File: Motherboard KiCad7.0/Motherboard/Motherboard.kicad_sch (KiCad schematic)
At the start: 74 parts, among them J1 USB_B_Micro, J2 SWD_01x04_Pin, J3 2-1445057-2, J4 2-1445057-2, J5 2-1445057-2, J6 2-1445057-2, J7 2-1445057-2, Q1 AO3400A, Q2 AO3400A, Q3 AO3400A, Q4 AO3400A, Q5 AO3400A, Q6 AO3400A, SW1 SW_STM_RESET, SW2 SW_STM_BOOT_MODE, U1 STM32F103CBT6, U2 AMS1117-3.3, U3 LM66100DCKR, U4 LM66100DCKR, U5 LM66100DCKR, Y1 X322516MMB4SI

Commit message: Added screwswitch and subsheet
Added screwswitch symbol and created a subsheet to place the rest of the circuit components into
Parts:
- removed BZ1: PKM13EPYH4000, footprints:Buzzer_12.6x9.5RM5.0, symbol Device:Buzzer
- removed D1, D10, D2, D6, D7, D8, D9: 1N5819WS, Diode_SMD:D_SOD-323, symbol Diode:1N5819WS
- removed D5: WS2812B, LED_SMD:LED_WS2812B_PLCC4_5.0x5.0mm_P3.2mm, symbol LED:WS2812B
- removed J3, J4, J5, J6, J7: 2-1445057-2, CONN_2-1445057-2_TYCO, symbol CONN_2-1445057-2_TYCO:2-1445057-2
- removed Q1, Q2, Q3, Q4, Q5, Q6: AO3400A, Package_TO_SOT_SMD:SOT-23, symbol Transistor_FET:AO3400A
- removed R10, R12, R14, R16, R18, R4: 510R, Resistor_SMD:R_0603_1608Metric, symbol Device:R
- removed R11, R13, R15, R17, R5, R9: 10k, Resistor_SMD:R_0603_1608Metric, symbol Device:R
- removed R7: 1k, Resistor_SMD:R_0603_1608Metric, symbol Device:R
- added C17: 4.7uF, Capacitor_SMD:C_0805_2012Metric, symbol Device:C
- added C18, C19: 100nF, Capacitor_SMD:C_0603_1608Metric, symbol Device:C
- added C20, C21: 22uF, Capacitor_SMD:C_0805_2012Metric, symbol Device:C
- added C22: 100uF, Capacitor_SMD:CP_Elec_6.3x5.9, symbol Device:C_Polarized
- added D11: WS2812B, LED_SMD:LED_WS2812B_PLCC4_5.0x5.0mm_P3.2mm, symbol LED:WS2812B
- added L1: 5.6uH, Inductor_SMD:L_Bourns_SRN8040TA, symbol Device:L
- added R19: 100k, Resistor_SMD:R_0603_1608Metric, symbol Device:R
- added R20: 22k, Resistor_SMD:R_0603_1608Metric, symbol Device:R
- added TP8: TP_BATT1, TestPoint:TestPoint_Pad_2.0x2.0mm, symbol Connector:TestPoint
- added TP9: TP_3.3V_A, TestPoint:TestPoint_Pad_2.0x2.0mm, symbol Connector:TestPoint
- added U6: LMR51430XDDCR, Package_TO_SOT_SMD:SOT-23-6_Handsoldering, symbol QRET_Buck_PSU-symbols:LMR51430XDDCR
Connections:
- net +3.3V: no longer D3.1 (VDD)
- net +BATT: now also C17.1, C18.1, TP8.1, U6.3 (VIN), U6.5 (EN)
- net GND: now also C17.2, C18.2, C20.2, C21.2, C22.2, D11.3 (VSS), R20.2, U6.1 (GND)
- net at D3.2 (DOUT): now also D11.4 (DIN)
- new net: C19.1, L1.1, U6.2 (SW)
- new net: C19.2, U6.6 (CB)
- new net: R19.2, R20.1, U6.4 (FB)
- new net 3.3V_A: C20.1, C21.1, C22.1, D11.1 (VDD), D3.1 (VDD), L1.2, R19.1, TP9.1
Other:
- added sheet Motherboard P2 (Motherboard P2.kicad_sch)
- note added: "FOLLOW LAYOUT EXAMPLE (9.4.2) FROM DATASHEET LMR51430: PFM @ 500kHz (simpler routing & higher efficiency)"
- note added: "Max Output: 2.5A"
- note added: "Primary 3.3V Buck Regulator"
- note added: "Rfbt=100k, Rfbb=22k Vout = ((Rfbt*0.6)/Rfbb)+0.6 Vout = 3.327V"
- note removed: "Air Pump"
- note removed: "Buzzer"
- note removed: "Solenoid Valves"
- moved on the sheet: C1, J2, R2, SW1

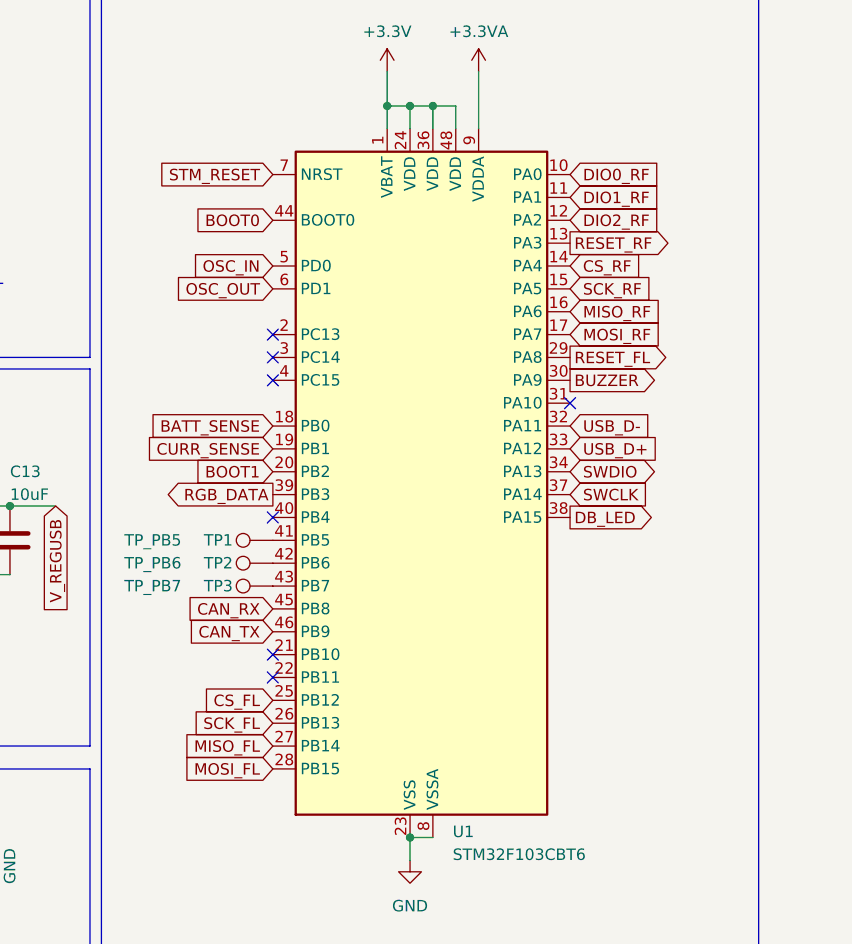
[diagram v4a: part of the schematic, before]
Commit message: Updated STM32 pinout
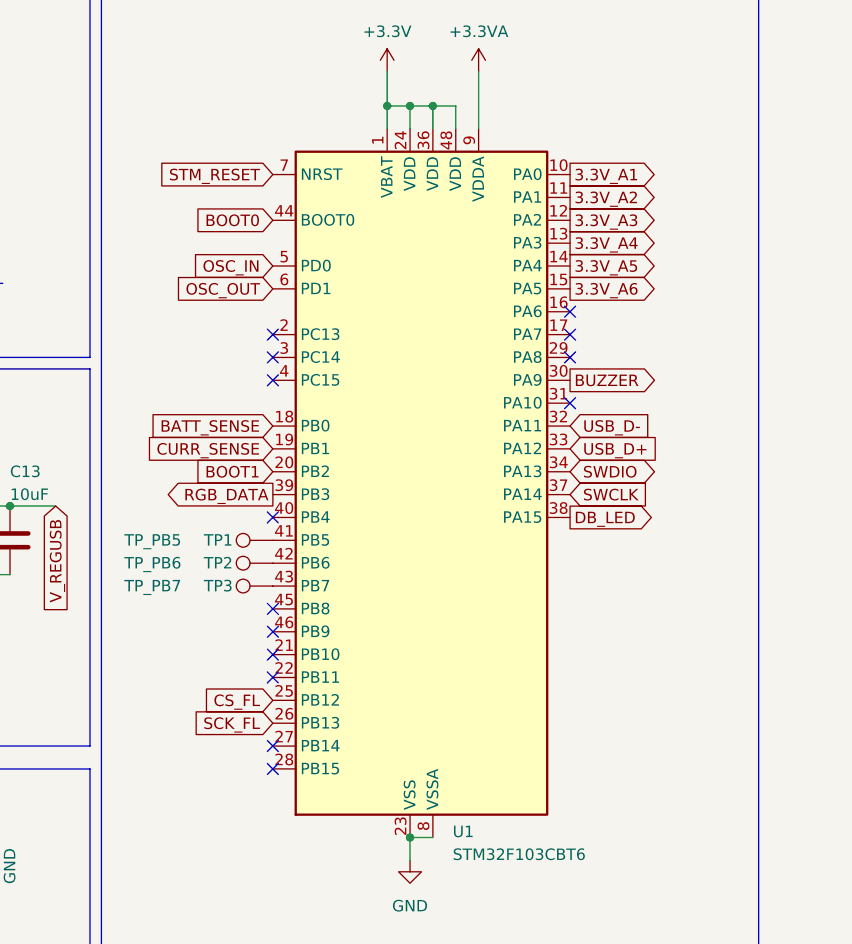
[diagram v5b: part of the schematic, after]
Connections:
- net CAN_RX: no longer names the net of U1.45 (PB8)
- net CAN_TX: no longer names the net of U1.46 (PB9)
- net CS_RF renamed 3.3V_A5
- net DIO0_RF renamed 3.3V_A1
- net DIO1_RF renamed 3.3V_A2
- net DIO2_RF renamed 3.3V_A3
- net MISO_FL: no longer names the net of U1.27 (PB14)
- net MISO_RF: no longer names the net of U1.16 (PA6)
- net MOSI_FL: no longer names the net of U1.28 (PB15)
- net MOSI_RF: no longer names the net of U1.17 (PA7)
- net RESET_FL: no longer names the net of U1.29 (PA8)
- net RESET_RF renamed 3.3V_A4
- net SCK_RF renamed 3.3V_A6
- no-connect marks 10 -> 17
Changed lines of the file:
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@@
   (junction (at 247.65 29.21) (diameter 0) (color 0 0 0 0)
   )
+  (no_connect (at 229.87 100.33))
   (no_connect (at 132.08 38.1))
+  (no_connect (at 229.87 87.63))
   (no_connect (at 229.87 59.69))
+  (no_connect (at 229.87 85.09))
   (no_connect (at 229.87 92.71))
   (no_connect (at 229.87 74.93))
+  (no_connect (at 229.87 102.87))
   (no_connect (at 162.56 83.82))
+  (no_connect (at 262.89 57.15))
+  (no_connect (at 262.89 52.07))
   (no_connect (at 262.89 62.23))
   (no_connect (at 229.87 54.61))
+  (no_connect (at 262.89 54.61))
   (no_connect (at 152.4 88.9))
   (no_connect (at 229.87 90.17))
@@
     )
   )
-  (global_label "RESET_RF" (shape output) (at 262.89 44.45 0) (fields_autoplaced)
-    (effects (font (size 1.27 1.27)) (justify left))
-    (property "Intersheetrefs" "${INTERSHEET_REFS}" (at 274.9465 44.45 0)
-      (effects (font (size 1.27 1.27)) (justify left) hide)
-    )
-  )
   (global_label "DB_LED" (shape input) (at 97.155 66.675 180) (fields_autoplaced)
     (effects (font (size 1.27 1.27)) (justify right))
@@
     )
   )
-  (global_label "CAN_RX" (shape input) (at 229.87 85.09 180) (fields_autoplaced)
-    (effects (font (size 1.27 1.27)) (justify right))
-    (property "Intersheetrefs" "${INTERSHEET_REFS}" (at 219.7486 85.09 0)
-      (effects (font (size 1.27 1.27)) (justify right) hide)
-    )
-  )
   (global_label "V_REGUSB" (shape input) (at 205.74 73.66 270) (fields_autoplaced)
     (effects (font (size 1.27 1.27)) (justify right))
@@
     )
   )
+  (global_label "3.3V_A1" (shape output) (at 262.89 36.83 0) (fields_autoplaced)
+    (effects (font (size 1.27 1.27)) (justify left))
+    (property "Intersheetrefs" "${INTERSHEET_REFS}" (at 273.2533 36.83 0)
+      (effects (font (size 1.27 1.27)) (justify left) hide)
+    )
+  )
   (global_label "OSC_OUT" (shape input) (at 229.87 49.53 180) (fields_autoplaced)
     (effects (font (size 1.27 1.27)) (justify right))
@@
     )
   )
-  (global_label "MISO_RF" (shape input) (at 262.89 52.07 0) (fields_autoplaced)
-    (effects (font (size 1.27 1.27)) (justify left))
-    (property "Intersheetrefs" "${INTERSHEET_REFS}" (at 273.7976 52.07 0)
-      (effects (font (size 1.27 1.27)) (justify left) hide)
-    )
-  )
-  (global_label "CAN_TX" (shape input) (at 229.87 87.63 180) (fields_autoplaced)
-    (effects (font (size 1.27 1.27)) (justify right))
-    (property "Intersheetrefs" "${INTERSHEET_REFS}" (at 220.051 87.63 0)
-      (effects (font (size 1.27 1.27)) (justify right) hide)
-    )
-  )
   (global_label "SCK_FL" (shape input) (at 229.87 97.79 180) (fields_autoplaced)
     (effects (font (size 1.27 1.27)) (justify right))
@@
     )
   )
-  (global_label "MOSI_RF" (shape input) (at 262.89 54.61 0) (fields_autoplaced)
-    (effects (font (size 1.27 1.27)) (justify left))
-    (property "Intersheetrefs" "${INTERSHEET_REFS}" (at 273.7976 54.61 0)
-      (effects (font (size 1.27 1.27)) (justify left) hide)
-    )
-  )
   (global_label "SWCLK" (shape input) (at 262.89 72.39 0) (fields_autoplaced)
     (effects (font (size 1.27 1.27)) (justify left))
@@
     )
   )
-  (global_label "RESET_FL" (shape output) (at 262.89 57.15 0) (fields_autoplaced)
-    (effects (font (size 1.27 1.27)) (justify left))
-    (property "Intersheetrefs" "${INTERSHEET_REFS}" (at 274.7046 57.15 0)
+  (global_label "3.3V_A3" (shape output) (at 262.89 41.91 0) (fields_autoplaced)
+    (effects (font (size 1.27 1.27)) (justify left))
+    (property "Intersheetrefs" "${INTERSHEET_REFS}" (at 273.2533 41.91 0)
       (effects (font (size 1.27 1.27)) (justify left) hide)
     )
@@
     )
   )
-  (global_label "DIO0_RF" (shape input) (at 262.89 36.83 0) (fields_autoplaced)
-    (effects (font (size 1.27 1.27)) (justify left))
-    (property "Intersheetrefs" "${INTERSHEET_REFS}" (at 273.6162 36.83 0)
+  (global_label "3.3V_A4" (shape output) (at 262.89 44.45 0) (fields_autoplaced)
+    (effects (font (size 1.27 1.27)) (justify left))
+    (property "Intersheetrefs" "${INTERSHEET_REFS}" (at 273.2533 44.45 0)
       (effects (font (size 1.27 1.27)) (justify left) hide)
     )
@@
     )
   )
-  (global_label "DIO1_RF" (shape input) (at 262.89 39.37 0) (fields_autoplaced)
-    (effects (font (size 1.27 1.27)) (justify left))
-    (property "Intersheetrefs" "${INTERSHEET_REFS}" (at 273.6162 39.37 0)
-      (effects (font (size 1.27 1.27)) (justify left) hide)
-    )
-  )
-  (global_label "DIO2_RF" (shape input) (at 262.89 41.91 0) (fields_autoplaced)
-    (effects (font (size 1.27 1.27)) (justify left))
-    (property "Intersheetrefs" "${INTERSHEET_REFS}" (at 273.6162 41.91 0)
-      (effects (font (size 1.27 1.27)) (justify left) hide)
-    )
-  )
   (global_label "STM_RESET" (shape output) (at 66.04 176.53 0) (fields_autoplaced)
     (effects (font (size 1.27 1.27)) (justify left))
@@
     )
   )
-  (global_label "CS_RF" (shape input) (at 262.89 46.99 0) (fields_autoplaced)
-    (effects (font (size 1.27 1.27)) (justify left))
-    (property "Intersheetrefs" "${INTERSHEET_REFS}" (at 271.6809 46.99 0)
+  (global_label "3.3V_A5" (shape output) (at 262.89 46.99 0) (fields_autoplaced)
+    (effects (font (size 1.27 1.27)) (justify left))
+    (property "Intersheetrefs" "${INTERSHEET_REFS}" (at 273.2533 46.99 0)
       (effects (font (size 1.27 1.27)) (justify left) hide)
     )
@@
     )
   )
-  (global_label "MOSI_FL" (shape input) (at 229.87 102.87 180) (fields_autoplaced)
-    (effects (font (size 1.27 1.27)) (justify right))
-    (property "Intersheetrefs" "${INTERSHEET_REFS}" (at 219.2043 102.87 0)
-      (effects (font (size 1.27 1.27)) (justify right) hide)
-    )
-  )
   (global_label "3.3V_A" (shape input) (at 101.6 30.48 180) (fields_autoplaced)
     (effects (font (size 1.27 1.27)) (justify right))
@@
     )
   )
-  (global_label "MISO_FL" (shape input) (at 229.87 100.33 180) (fields_autoplaced)
-    (effects (font (size 1.27 1.27)) (justify right))
-    (property "Intersheetrefs" "${INTERSHEET_REFS}" (at 219.2043 100.33 0)
-      (effects (font (size 1.27 1.27)) (justify right) hide)
-    )
-  )
   (global_label "BOOT0" (shape input) (at 229.87 41.91 180) (fields_autoplaced)
     (effects (font (size 1.27 1.27)) (justify right))
@@
     )
   )
+  (global_label "3.3V_A6" (shape output) (at 262.89 49.53 0) (fields_autoplaced)
+    (effects (font (size 1.27 1.27)) (justify left))
+    (property "Intersheetrefs" "${INTERSHEET_REFS}" (at 273.2533 49.53 0)
+      (effects (font (size 1.27 1.27)) (justify left) hide)
+    )
+  )
   (global_label "SWCLK" (shape input) (at 49.53 144.78 180) (fields_autoplaced)
     (effects (font (size 1.27 1.27)) (justify right))
@@
     )
   )
-  (global_label "SCK_RF" (shape input) (at 262.89 49.53 0) (fields_autoplaced)
-    (effects (font (size 1.27 1.27)) (justify left))
-    (property "Intersheetrefs" "${INTERSHEET_REFS}" (at 272.9509 49.53 0)
-      (effects (font (size 1.27 1.27)) (justify left) hide)
-    )
-  )
   (global_label "USB_D-" (shape input) (at 165.1 81.28 270) (fields_autoplaced)
     (effects (font (size 1.27 1.27)) (justify right))
@@
     )
   )
+  (global_label "3.3V_A2" (shape output) (at 262.89 39.37 0) (fields_autoplaced)
+    (effects (font (size 1.27 1.27)) (justify left))
+    (property "Intersheetrefs" "${INTERSHEET_REFS}" (at 273.2533 39.37 0)
+      (effects (font (size 1.27 1.27)) (justify left) hide)
+    )
+  )

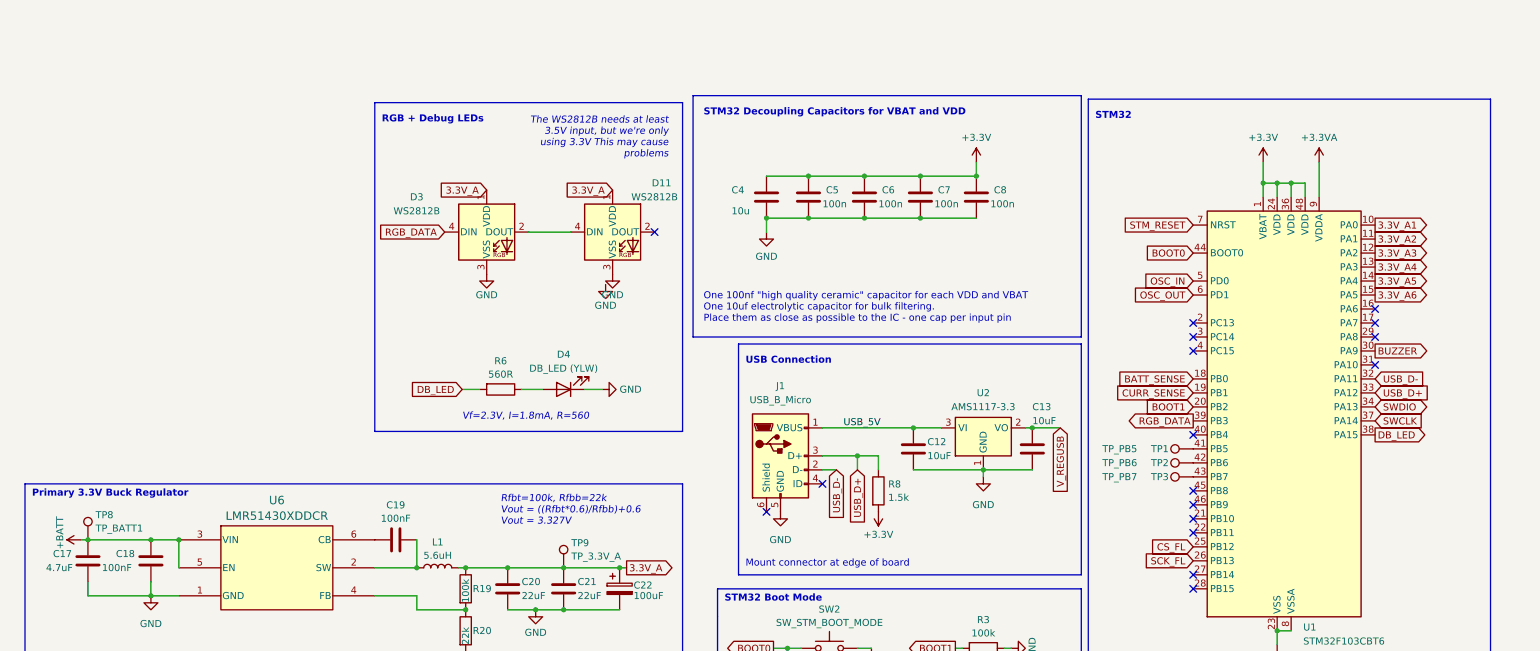
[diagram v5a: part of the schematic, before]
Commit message: Updated power connectors
Updated power connectors. Updated symbols and footprints for all components copied from avionics communications module.
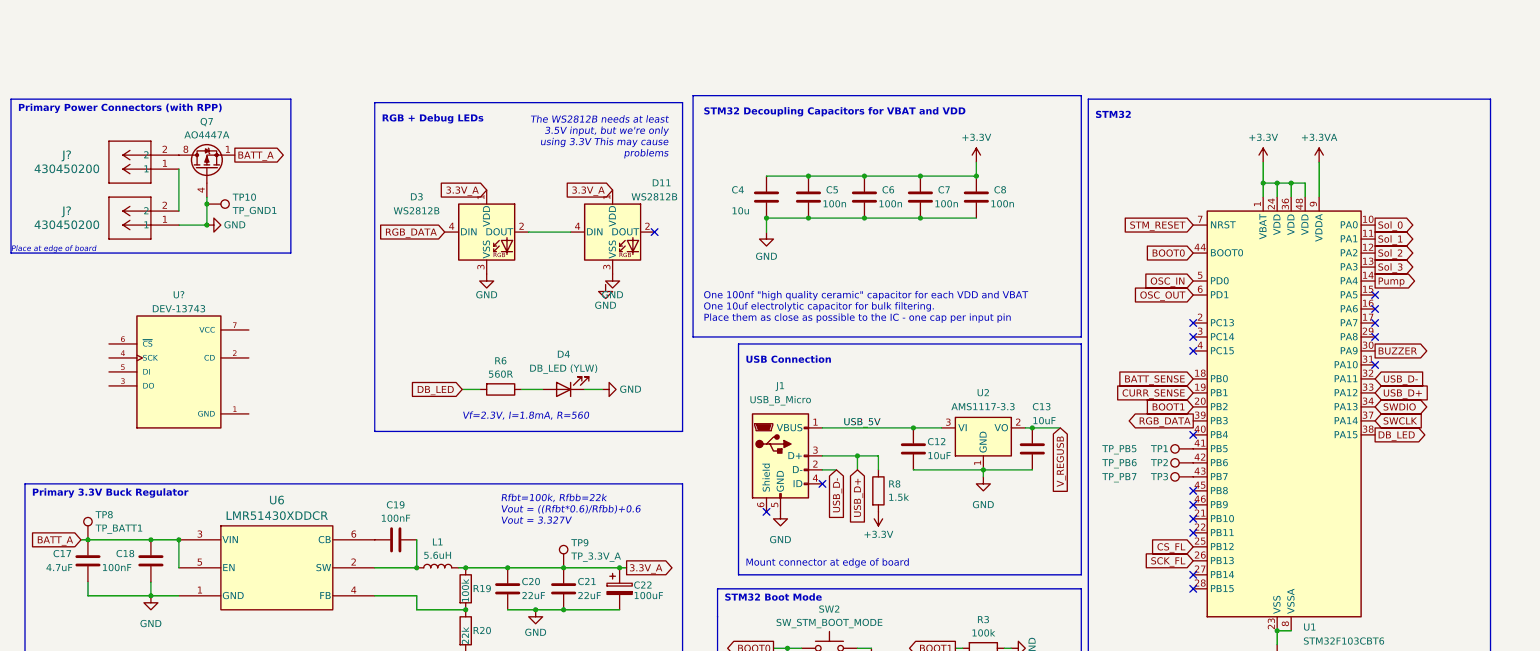
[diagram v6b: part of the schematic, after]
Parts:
- added J? (x2): 430450200, CONN 0430450200:CON_430450200_MOL, symbol CONN 0430450200:430450200
- added Q7: AO4447A, Package_SO:SOIC-8_3.9x4.9mm_P1.27mm, symbol Transistor_FET:IRF7404
- added TP10: TP_GND1, TestPoint:TestPoint_Pad_2.0x2.0mm, symbol Connector:TestPoint
- added U?: DEV-13743, DEV-13743:MODULE_DEV-13743, symbol DEV-13743:DEV-13743
- C10, C11: Digikey 732-8541-1-ND -> (none); LCSC (none) -> C28323
- D11, D3: Digikey (none) -> 1568-COM-16347CT-ND
- J2: Digikey (none) -> 2057-PH1RB-04-UA-ND
- SW1, SW2: Digikey PTS636 SK43 SMTR LFS -> (none); LCSC (none) -> C318884
- U3, U4, U5: Digikey 296-53541-1-ND -> (none); LCSC (none) -> C2869734
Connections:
- net GND: now also J?.1, Q7.4 (G), TP10.1
- net +BATT renamed BATT_A
- net BATT_A: now also Q7.1 (S), Q7.2 (S), Q7.3 (S)
- net 3.3V_A1 renamed Sol_0
- net 3.3V_A2 renamed Sol_1
- net 3.3V_A3 renamed Sol_2
- net 3.3V_A4 renamed Sol_3
- net 3.3V_A5 renamed Pump
- net 3.3V_A6: no longer names the net of U1.15 (PA5)
- new net: J?.1, J?.2
- new net: J?.2, Q7.5 (D), Q7.6 (D), Q7.7 (D), Q7.8 (D)
- no-connect marks 17 -> 18
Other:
- note added: "Place at edge of board"
- note added: "Primary Power Connectors (with RPP)"
